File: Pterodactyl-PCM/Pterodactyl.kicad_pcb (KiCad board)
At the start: 2 copper layers, 45 x 32.5 mm, 18 parts, among them J1 Left Header, U1 PCM512x

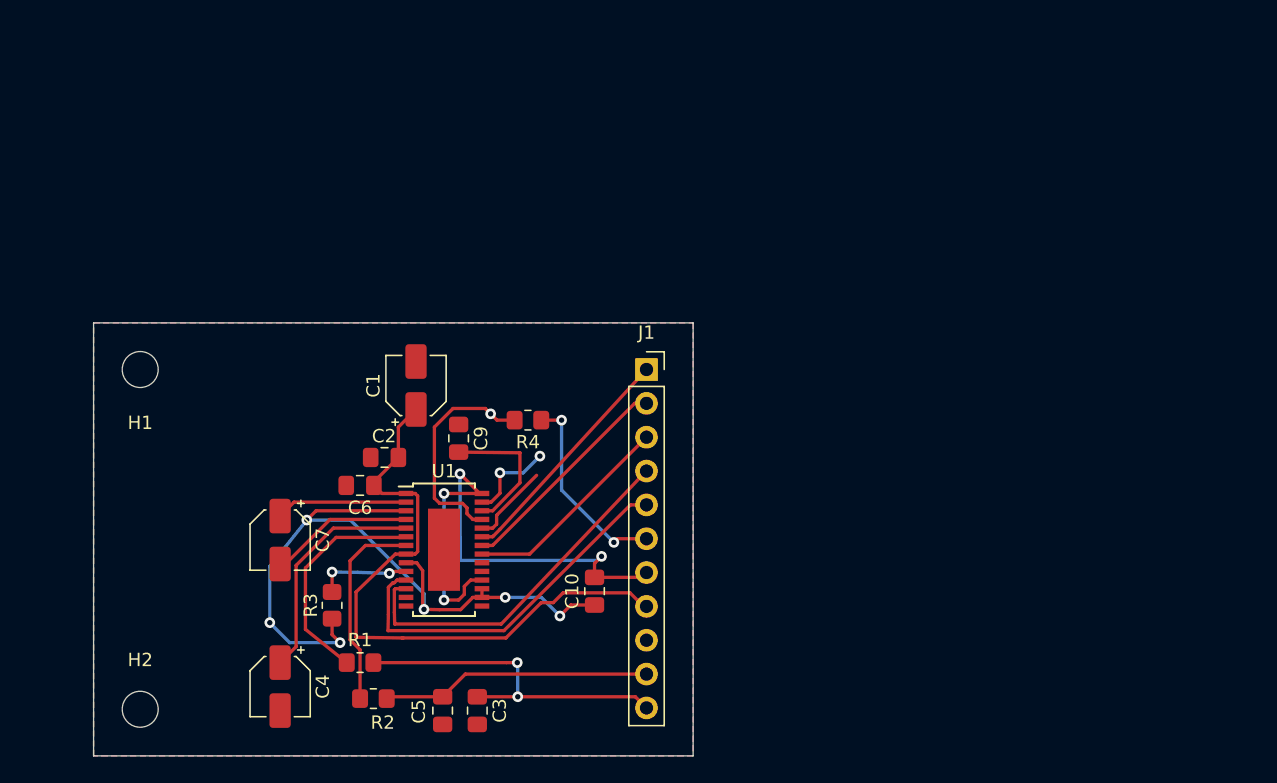
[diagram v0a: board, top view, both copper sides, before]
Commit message: added DC regulator
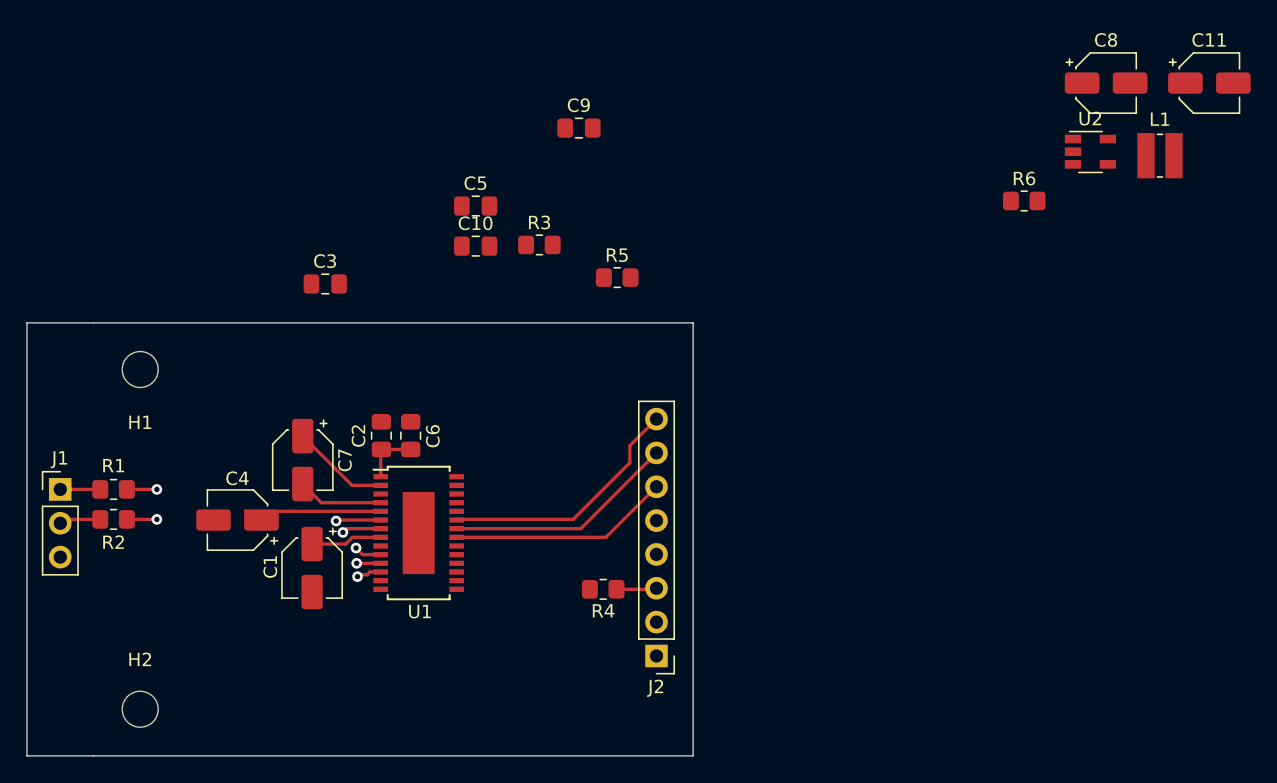
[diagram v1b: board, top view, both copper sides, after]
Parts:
- added C11: 10U, Capacitor_SMD:CP_Elec_4x4.5, F.Cu at (218.8, 74.5)
- added C8: 4.7U, Capacitor_SMD:CP_Elec_4x4.5, F.Cu at (211.0, 74.5)
- added J2: Conn_01x08_Male, Connector_PinHeader_2.54mm:PinHeader_1x08_P2.54mm_Vertical, F.Cu at (177.2, 117.5)
- added L1: 2.2U, Inductor_SMD:L_Wuerth_MAPI-3015, F.Cu at (215.0, 80.0)
- added R6: 100K, Resistor_SMD:R_0805_2012Metric_Pad1.20x1.40mm_HandSolder, F.Cu at (204.8, 83.3)
- added U2: LM3670MF, Package_TO_SOT_SMD:TSOT-23-5, F.Cu at (209.8, 79.7)
- J1: value Left Header -> Conn_01x03_Male; footprint Connector_PinSocket_2.54mm:PinSocket_1x11_P2.54mm_Vertical -> Connector_PinHeader_2.54mm:PinHeader_1x03_P2.54mm_Vertical
- R5: moved to F.Cu
- moved J1 44.9 mm to (132.5, 105.0)
- moved C5 38.0 mm to (163.7, 83.7), turned to 0 degrees
- moved C3 34.0 mm to (152.4, 89.6), turned to 0 degrees
- moved R3 31.2 mm to (168.5, 86.7), turned to 0 degrees
- moved C10 27.4 mm to (163.7, 86.7), turned to 0 degrees
- moved C9 25.0 mm to (171.4, 77.9), turned to 0 degrees
- moved R5 24.4 mm to (174.3, 89.1), turned to 0 degrees
- moved R2 23.7 mm to (136.5, 107.2), turned to 0 degrees
- moved R1 22.6 mm to (136.5, 105.0), turned to 180 degrees
- moved C1 15.8 mm to (151.4, 110.9), turned to 270 degrees
- moved R4 13.9 mm to (173.2, 112.5)
- moved C4 12.9 mm to (145.8, 107.3), turned to 180 degrees
- moved C7 6.24 mm to (150.7, 102.8)
- moved C6 5.33 mm to (158.8, 101.0), turned to 90 degrees
- moved U1 2.28 mm to (159.4, 108.3)
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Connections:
- C1 pad 1: +3.3VADC -> /VCC
- C10 pad 2: +3.3VDAC -> +3V3
- C2 pad 1: +3.3VADC -> /VCC
- C6 pad 1: +3.3VADC -> /VCC
- J1 pad 1: /LRCK -> OUTL
- J1 pad 2: /DIN -> OUTR
- J1 pad 3: /BCK -> GND
- R5 pad 1: +3.3VDAC -> +3V3
- U1 pad 1: +3.3VADC -> /VCC
- U1 pad 28: +3.3VDAC -> +3V3
- U1 pad 8: +3.3VADC -> /VCC
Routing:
- net GND: track 69.0 -> 0.00 mm, vias 8 -> 0
- net +3.3VADC: track 48.4 -> 0.00 mm
- net +3.3VDAC: track 32.3 -> 0.00 mm, vias 3 -> 0
- net /SDA: track 28.2 -> 1.80 mm, vias 0 -> 1
- net /SCL: track 27.3 -> 1.98 mm, vias 0 -> 1
- net OUTL: track 26.4 -> 3.00 mm, vias 2 -> 0
- net OUTR: track 20.4 -> 3.12 mm
- net Net-(R4-Pad2): track 16.8 -> 0.00 mm, vias 1 -> 0
- net /MUTE: track 14.9 -> 3.03 mm, vias 2 -> 0
- net Net-(R1-Pad1): track 17.1 -> 5.67 mm, vias 0 -> 2
- net Net-(C9-Pad2): track 10.6 -> 0.00 mm
- net Net-(R2-Pad2): track 15.3 -> 5.24 mm, vias 0 -> 2
- net /VCC: track 0.00 -> 9.63 mm
- net Net-(C4-Pad1): track 17.7 -> 9.29 mm
- net Net-(R5-Pad2): track 6.36 -> 0.00 mm, vias 1 -> 0
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- removed copper zone on B.Cu, net GND
- removed copper zone on F.Cu, net GND
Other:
- board size 45 x 32.5 mm -> 50 x 32.5 mm
